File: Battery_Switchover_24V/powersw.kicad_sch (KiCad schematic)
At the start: 28 parts, among them J2 430450612, J4 430450612, J5 430450612, Q6 FDBL86066-F085, Q7 FDBL86066-F085, U16 LM74610QDGKRQ1, U6 LM74610QDGKRQ1, U7 FDBL86066-F085

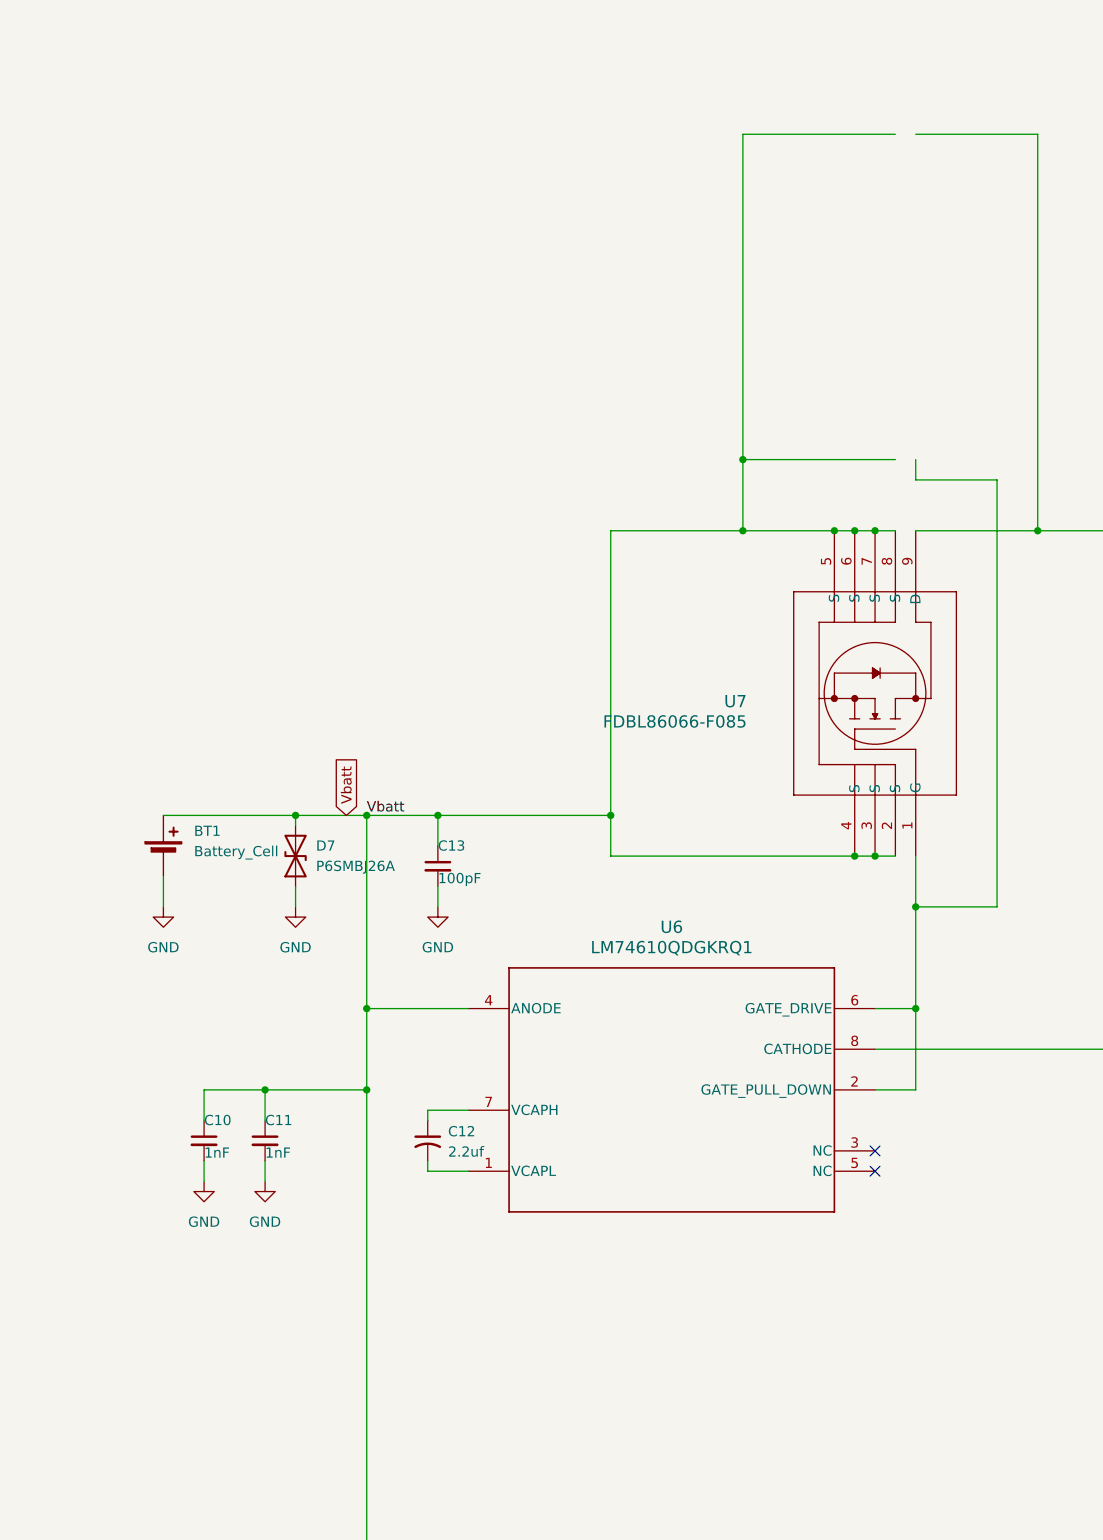
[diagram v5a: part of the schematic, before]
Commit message: Batt current monitor IC added, batt moved to charger page
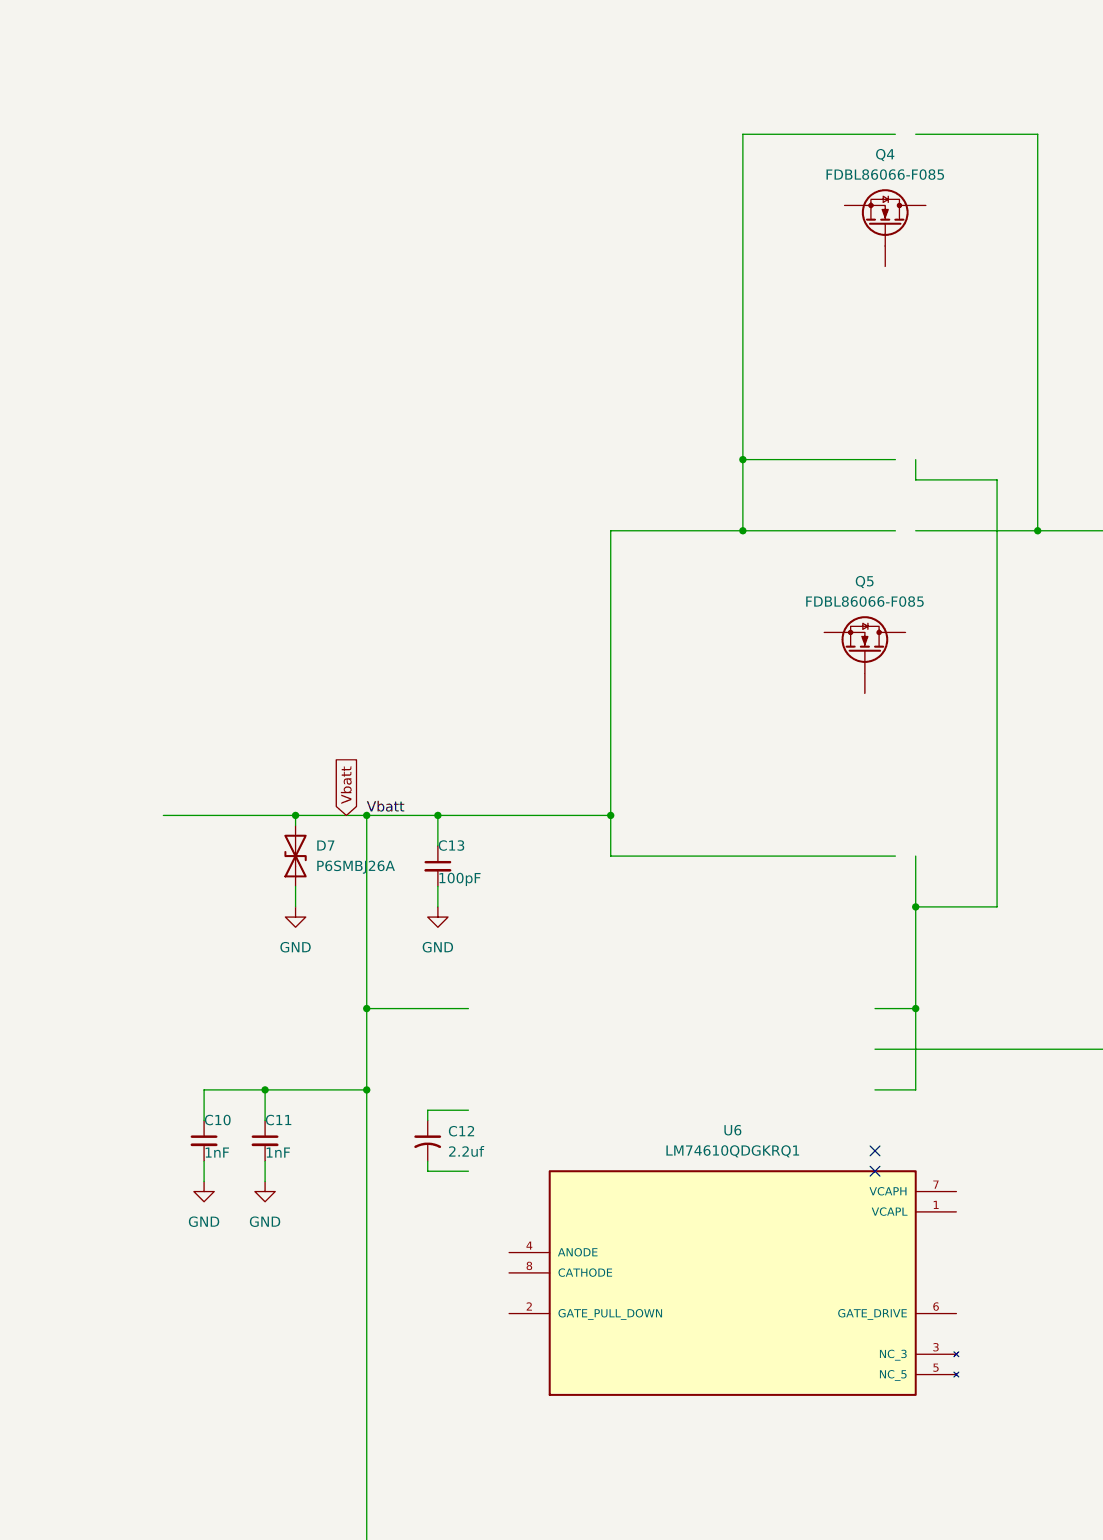
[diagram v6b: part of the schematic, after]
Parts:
- removed BT1: Battery_Cell, TerminalBlock_RND:TerminalBlock_RND_205-00023_1x02_P10.00mm_Horizontal, symbol Device:Battery_Cell
- removed U6: LM74610QDGKRQ1, footprints:DGK0008A_N, symbol LM74610:LM74610QDGKRQ1
- removed U7: FDBL86066-F085, H-PSOF8L_ONS, symbol FDBL86062:FDBL86066-F085
- added Q4, Q5: FDBL86066-F085, Package_TO_SOT_SMD:Infineon_PG-HSOF-8-1_ThermalVias, symbol Device:Q_NMOS
- added U6: LM74610QDGKRQ1, Package_SO:VSSOP-8_3x3mm_P0.65mm, symbol LM74610QDGKRQ1:LM74610QDGKRQ1
- Q6, Q7: footprint H-PSOF8L_ONS -> Package_TO_SOT_SMD:Infineon_PG-HSOF-8-1_ThermalVias
- U16: footprint LM74610QDGKRQ1:SOP65P490X110-8N -> Package_SO:VSSOP-8_3x3mm_P0.65mm

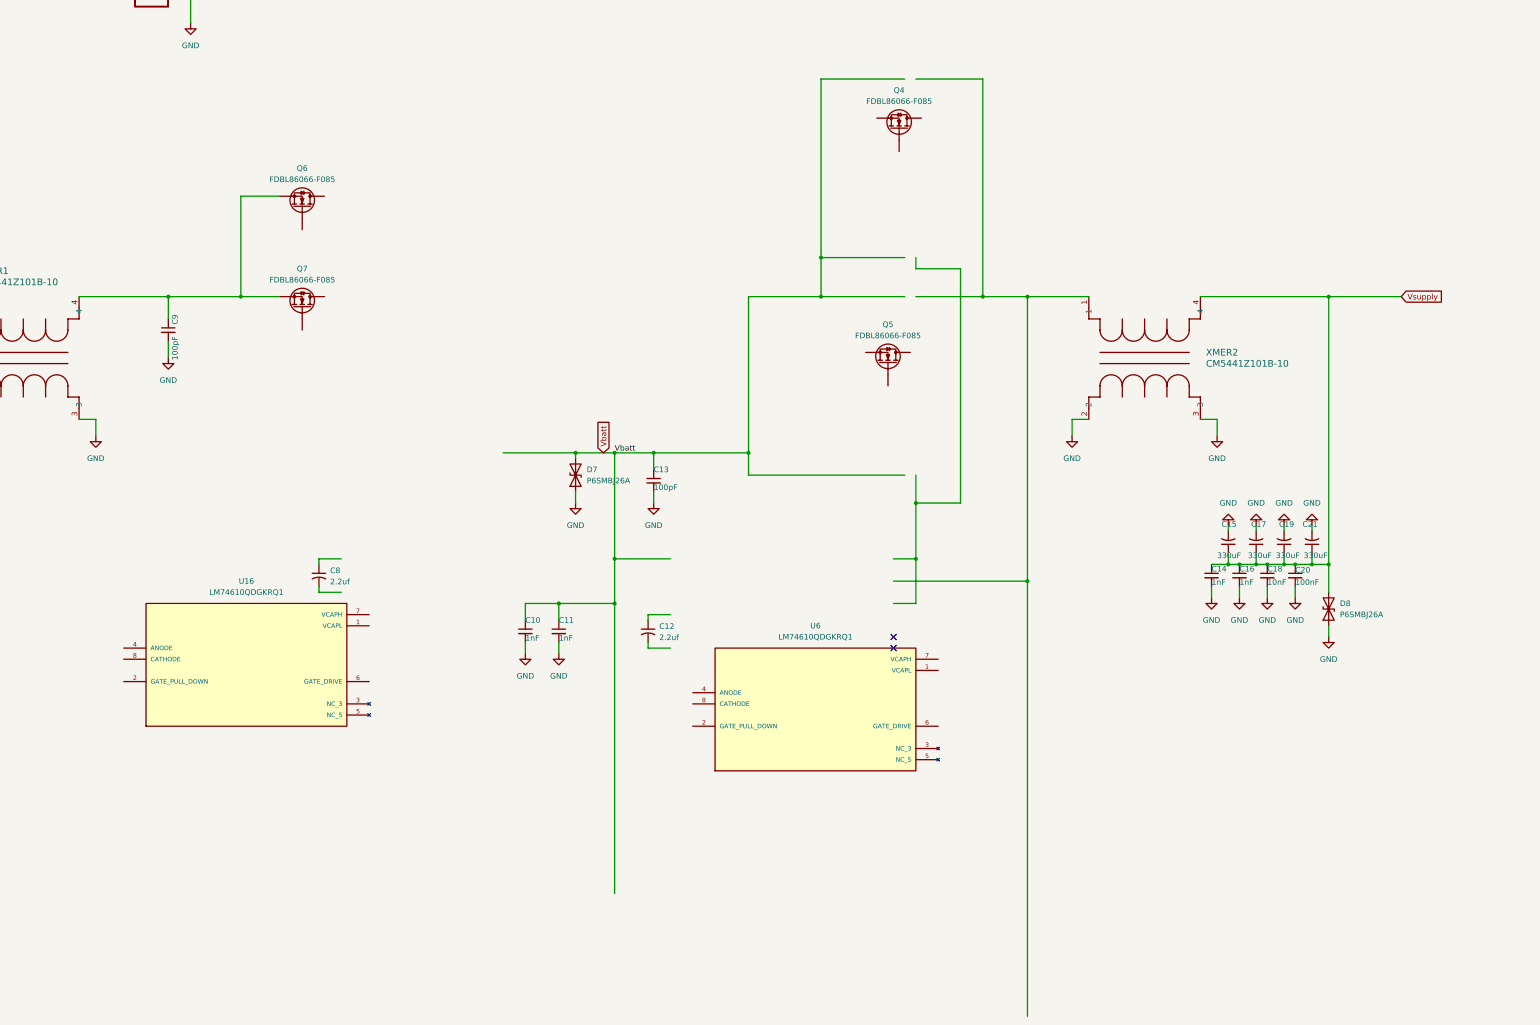
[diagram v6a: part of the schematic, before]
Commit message: Fixed the power switching added 2 100nF caps to battery charger buck converter
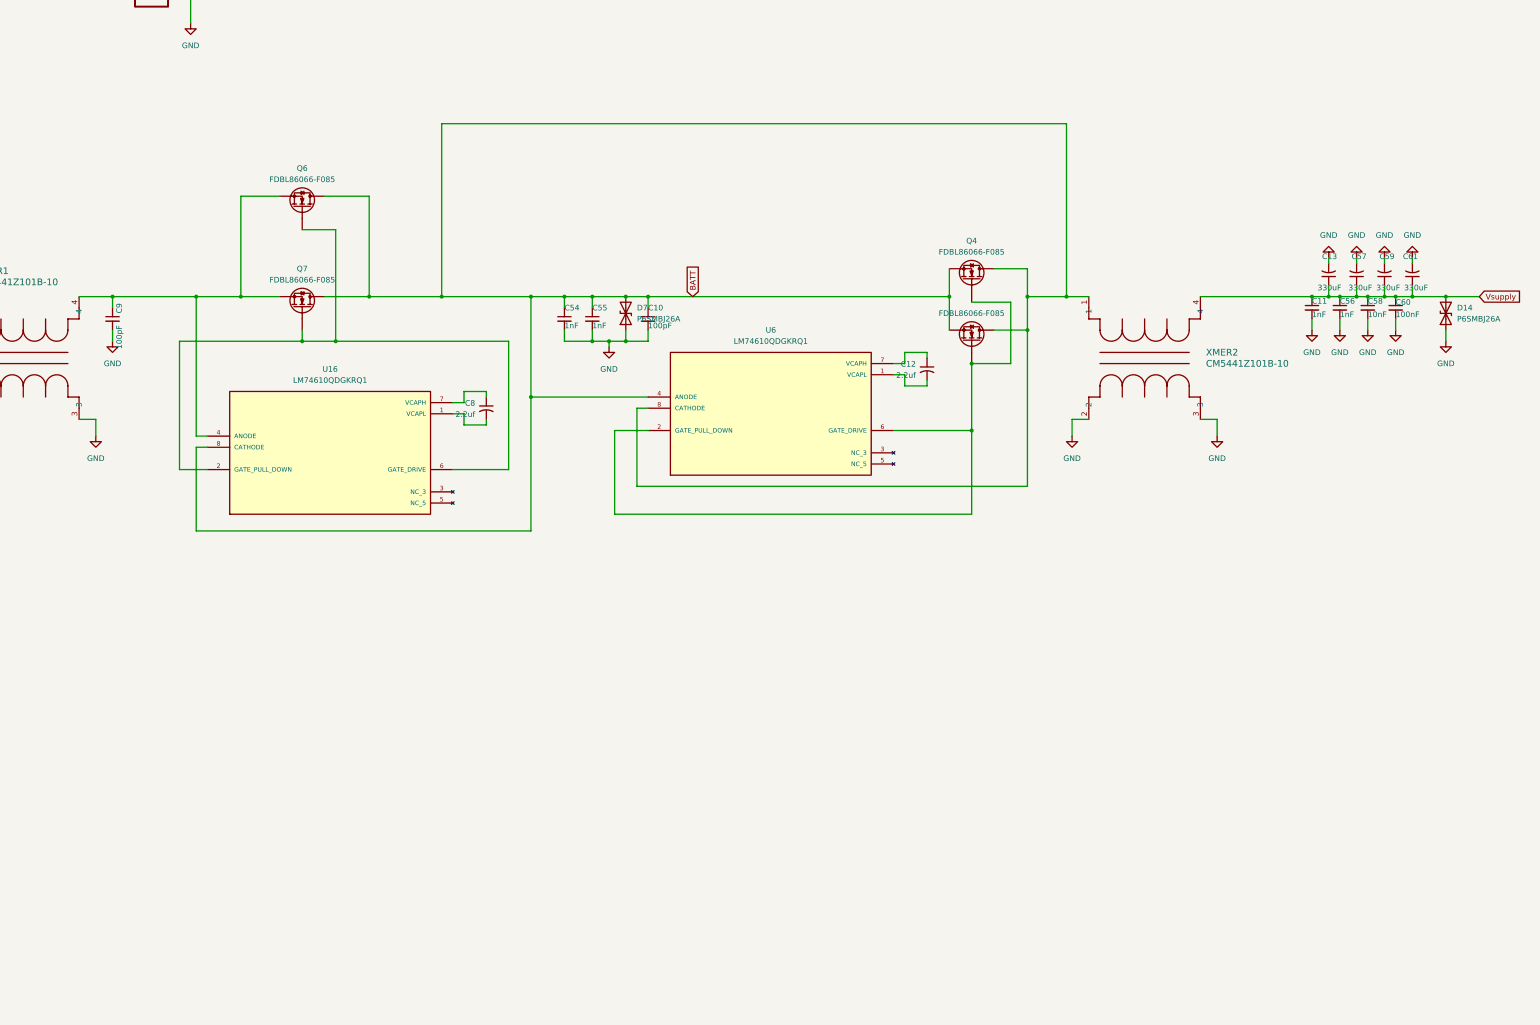
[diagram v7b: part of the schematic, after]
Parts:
- removed C13: 100pF, Capacitor_SMD:C_0603_1608Metric, symbol Device:C_Small
- removed C14, C16: 1nF, Capacitor_SMD:C_0402_1005Metric, symbol Device:C_Small
- removed C15, C17, C19, C21: 330uF, Capacitor_THT:CP_Radial_Tantal_D10.5mm_P5.00mm, symbol Device:C_Small_US
- removed C18: 10nF, Capacitor_SMD:C_0603_1608Metric, symbol Device:C_Small
- removed C20: 100nF, Capacitor_SMD:C_0603_1608Metric, symbol Device:C_Small
- removed D8: P6SMBJ26A, footprints:P26_DO-214AA_SMB, symbol Device:D_TVS
- added C13, C57, C59, C61: 330uF, Capacitor_THT:CP_Radial_Tantal_D10.5mm_P5.00mm, symbol Device:C_Small_US
- added C54, C55: 1nF, Capacitor_SMD:C_0603_1608Metric, symbol Device:C_Small
- added C56: 1nF, Capacitor_SMD:C_0402_1005Metric, symbol Device:C_Small
- added C58: 10nF, Capacitor_SMD:C_0603_1608Metric, symbol Device:C_Small
- added C60: 100nF, Capacitor_SMD:C_0603_1608Metric, symbol Device:C_Small
- added D14: P6SMBJ26A, footprints:P26_DO-214AA_SMB, symbol Device:D_TVS
- C10: value 1nF -> 100pF
- C11: footprint Capacitor_SMD:C_0603_1608Metric -> Capacitor_SMD:C_0402_1005Metric
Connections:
- net GND: now also C13.2, C54.2, C55.2, C56.2, C57.2, C58.2, C59.2, C60.2, C61.2, D14.1 (A1)
- net Vsupply: now also C11.1, C13.1, C56.1, C57.1, C58.1, C59.1, C60.1, C61.1, D14.2 (A2)
- net BATT: now reaches Q7.D
- net BATT: now also C10.1, D7.2 (A2), Q4.D, Q4.S, Q5.D, Q5.S, Q6.D, U16.8 (CATHODE), U6.4 (ANODE), U6.8 (CATHODE), XMER2.1, C54.1, C55.1
- net at Q7.G: now also Q6.G, U16.2 (GATE_PULL_DOWN), U16.6 (GATE_DRIVE)
- net at C9.1, Q6.S, Q7.S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: now also U16.4 (ANODE)
- net at Q4.G: now also Q5.G, U6.2 (GATE_PULL_DOWN), U6.6 (GATE_DRIVE)
- net at C8.1: now also U16.7 (VCAPH)
- net at C8.2: now also U16.1 (VCAPL)
- net at C12.1: now also U6.7 (VCAPH)
- net at C12.2: now also U6.1 (VCAPL)
- removed net Vbatt: C10.1, C11.1, D7.2 (A2)
- no-connect marks 2 -> 0
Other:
- moved on the sheet: C8, C9, D7, Q4, U16, U6

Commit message: Modified power switch sch
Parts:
- removed J2, J4, J5: 430450612, footprints:CONN_SD-43045-005_06_MOL, symbol 3X2MOLEX:430450612
- added J10, J11, J12, J13, J8, J9: ATX_2X3, Connector_Molex:Molex_Mini-Fit_Jr_5566-06A_2x03_P4.20mm_Vertical, symbol Connector_Generic:Conn_02x03_Top_Bottom
- added J7: Conn_01x02, symbol Connector_Generic:Conn_01x02
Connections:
- net GND: no longer C11.2, C13.2, C56.2, C57.2, C58.2, C59.2, C60.2, C61.2, D14.1 (A1), D6.1 (A1), XMER1.2, XMER2.3
- net VIN: now reaches C9.1, Q6.S, Q7.S, U16.4 (ANODE), XMER1.4
- net BATT: no longer names the net of C10.1, C54.1, C55.1, D7.2 (A2), Q4.D, Q5.D, Q6.D, Q7.D, U16.8 (CATHODE), U6.8 (CATHODE), XMER2.1
- net BATT: no longer Q4.S, Q5.S, U6.4 (ANODE)
- net Vin: no longer names the net of D6.2 (A2), XMER1.1
- net Vin: now also J7.1 (Pin_1)
- net Vsupply renamed VOUT
- net VOUT: now also J10.4 (Pin_4), J10.5 (Pin_5), J10.6 (Pin_6), J11.4 (Pin_4), J11.5 (Pin_5), J11.6 (Pin_6), J12.4 (Pin_4), J12.5 (Pin_5), J12.6 (Pin_6), J13.4 (Pin_4), J13.5 (Pin_5), J13.6 (Pin_6), J8.4 (Pin_4), J8.5 (Pin_5), J8.6 (Pin_6), J9.4 (Pin_4), J9.5 (Pin_5), J9.6 (Pin_6)
- new net: D6.1 (A1), J7.2 (Pin_2), XMER1.2
- new net LOAD1_GND_RETURN: J8.1 (Pin_1), J8.2 (Pin_2), J8.3 (Pin_3), J9.1 (Pin_1), J9.2 (Pin_2), J9.3 (Pin_3)
- new net LOAD2_GND_RETURN: J10.1 (Pin_1), J10.2 (Pin_2), J10.3 (Pin_3), J11.1 (Pin_1), J11.2 (Pin_2), J11.3 (Pin_3)
- new net LOAD3_GND_RETURN: J12.1 (Pin_1), J12.2 (Pin_2), J12.3 (Pin_3), J13.1 (Pin_1), J13.2 (Pin_2), J13.3 (Pin_3)
- new net VBATT: Q4.S, Q5.S, U6.4 (ANODE)
- new net VOUT_GNDPWR: C11.2, C13.2, C56.2, C57.2, C58.2, C59.2, C60.2, C61.2, D14.1 (A1), XMER2.3
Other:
- note added: "BATT SWITCH (ON WHEN VIN IS BELOW VBATT)"
- note added: "MAIN SWITCH (ON WHEN VIN POWERED)"
- note added: "OUT1"
- note added: "OUT2"
- note added: "OUT3"
- moved on the sheet: C10, C11, C12, C13, C54, C55, C56, C57, C58, C59, C60, C61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
